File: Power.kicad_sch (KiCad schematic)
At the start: 50 parts, among them Q1 FDN86246, Q2 VOS617A-7T, T1 POE70P-50L, U1 TPS23753APW, U3 TLV431ACDBZR

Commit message: all parts geo-renamed
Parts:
- renumbered C18 to 1C1, C6 to 1C2, C5 to 1C4, C2 to 1C6, C10 to 1C7, C1 to 1C8, D4 to 1D1, D8 to 1D2, L1 to 1L1, R7 to 1R1, T1 to 1T1, C15 to 2C1, C17 to 2C11, C8 to 2C17, C14 to 2C2, C4 to 2C3, C3 to 2C4, C11 to 2C5, C13 to 2C6, C7 to 2C7, C12 to 2C8, C9 to 2C9, D3 to 2D1, D5 to 2D2, D9 to 2D3, D10 to 2D4, D6 to 2D5, D2 to 2D6, Q2 to 2Q1, Q1 to 2Q2, R18 to 2R1, R15 to 2R10, R17 to 2R11, R11 to 2R12, R8 to 2R14, R12 to 2R2, R3 to 2R21, R5 to 2R22, R1 to 2R23, R6 to 2R24, R2 to 2R25, R44 to 2R3, R9 to 2R4, R13 to 2R5, R10 to 2R6, R4 to 2R7, R16 to 2R8, R21 to 2R9, U3 to 2U1, U1 to 2U2

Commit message: properties cleanup added unique parts ID
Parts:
- 1C1, 1C2: IDAnything (none) -> 8vn418a9pwjm9b23z3yyc8b216
- 1C4: IDAnything (none) -> bccken80nrg3qa7p21h7mkcjhb
- 1C6: IDAnything (none) -> 7bve16b3npknhberdk72je696f
- 1C7: IDAnything (none) -> 3z34bstg58g3zbj6bm49cfkw50
- 1C8: IDAnything (none) -> cjbd17kqpcg079c1ae8a37wt8d
- 1D1, 1D2: IDAnything (none) -> 0r5rb2gfdykaebc85bfax6x5f2
- 1L1: IDAnything (none) -> dbn5brktrjgv9av8fstr2zcje2
- 1R1: IDAnything (none) -> f6xf1ty46ajjx8stx2pw0mweha
- 1T1: IDAnything (none) -> e7yraqef2wh4eb3jmdjy5syben; IDAnything.Var (none) -> 3.3V(erq4zdb9s4hn19b3b16cprkhzt) 5V(e7yraqef2wh4eb3jmdjy5sy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
- 2C1: IDAnything (none) -> 72ex9h1b3mkkna04sc27d3hgfj
- 2C11, 2C4: IDAnything (none) -> 812ahgx2bmk3ebs6aawcaegb7n
- 2C17: IDAnything (none) -> 59pk20syfekmjadzqyyhdbv6d4
- 2C2: IDAnything (none) -> e5kfcvbxymkwra6w8qtzj3bv2h
- 2C3: IDAnything (none) -> 3mjnpw664cjjwa4yweaynntky6
- 2C5: IDAnything (none) -> f5rakc2bw6gvc87xd8jq7r93dj
- 2C6: IDAnything (none) -> 8sc04c0ze2kfx9x5k0dj01hj4j; IDAnything.Var (none) -> 3.3V(dj5t5bmsfrgfk9cbrcgdwvhyzh) 5V(8sc04c0ze2kfx9x5k0dj01h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
- 2C7: IDAnything (none) -> 5cec8xb21wkrn9jazn0tx4yt0k
- 2C8: IDAnything (none) -> cp71jb8htmjycabjvbztj9p7aw; IDAnything.Var (none) -> 3.3V(eycg0pb0zeg5q8gbfaje4hcqkk) 5V(cp71jb8htmjycabjvbztj9p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
- 2C9: IDAnything (none) -> aqwrz00jgagpg96skhayteyvza
- 2D1: IDAnything (none) -> 3evttnjk9mjpxbyr5j5d5v7g5p
- 2D2, 2D6: IDAnything (none) -> a0668b16k0g1k959tcdyk7ydbv
- 2D3: IDAnything (none) -> 82n9ztys7pjjma8ncwczfamr62
- 2D4: IDAnything (none) -> 6yy5yjp69ph2mbefj7c13n8ymr
- 2D5: IDAnything (none) -> arf6h94jkrjsd8gf0mkfyad9b2
- 2Q1: IDAnything (none) -> ck5h9cq90mkv8ar3c2x7c5qz0c
- 2Q2: IDAnything (none) -> evtxn9kt5gk1y9gmvvka18a8hf
- 2R1: IDAnything (none) -> ftsp2a555thn6bt15g7x2jan0j
- 2R10: IDAnything (none) -> 4g20wes274jns9jencm9th8va1
- 2R11: IDAnything (none) -> 9wnk69v9dyh8a9739d0j8yezqn; IDAnything.Var (none) -> 3.3V(1yn3h33r3mkcaag9zy18qnt9dx) 5V(9wnk69v9dyh8a9739d0j8ye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
- 2R12: IDAnything (none) -> 26egdzngepjd69cx08s4ysz9m1
- 2R14, 2R4: IDAnything (none) -> 51rzmzs5b4j9y8fva05p13xw6s
- 2R2: IDAnything (none) -> 0ytke1xmp8j7w8gr20m1x2j7jv; IDAnything.Var (none) -> 3.3V(19kmsbbs8jjt68bjd3tyb4xmac) 5V(0ytke1xmp8j7w8gr20m1x2j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
- 2R21: IDAnything (none) -> 6gdsv03sw0gm694qqm04v6grhn
- 2R22: IDAnything (none) -> 52g08xz0vyhy08q0wme80j1vq0
- 2R23, 2R24: IDAnything (none) -> dyjzv1pb1rkbh96xb831vxg5z5
- 2R25: IDAnything (none) -> 7qxded0vrjg52ba46ry138eh06
- 2R3: IDAnything (none) -> 1wmdmcdgcmj9c8938zdzzabcvk
- 2R5: IDAnything (none) -> c1vc3q1ecwg38aepd291cy2avj
- 2R6: IDAnything (none) -> 3g0t5qb6k0gw2bj7sxecxs6d79
- 2R7: IDAnything (none) -> 27n3c98cw6kjv9d2ecsc87yqk3
- 2R8: IDAnything (none) -> 8katcbe2c2g6v9h87qywc7zr1y; IDAnything.Var (none) -> 3.3V(bpwqf11a58g6vacwyq9nfpvkjf) 5V(8katcbe2c2g6v9h87qywc7z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
- 2R9: IDAnything (none) -> 9p42scdygwgwrb2y4eq9ka8qyv; IDAnything.Var (none) -> 3.3V(19kmsbbs8jjt68bjd3tyb4xmac) 5V(9p42scdygwgwrb2y4eq9ka8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
- 2U1: IDAnything (none) -> 8fydhve1t4g9rbpgbwj8xzad8w
- 2U2: Availability In Stock -> (none); Check_prices https://www.snapeda.com/parts/TPS23753APW/Texas+Instruments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 -> (none); Description_1 IEEE 802.3-2005 PoE interface and Isolated Converter contro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 -> (none); IDAnything (none) -> 5jk78tnpyggbgbqs9p2kxsxakc; MF Texas Instruments -> (none); MP TPS23753APW -> (none); Package TSSOP-14 Texas Instruments -> (none); Price None -> (none); SnapEDA_Link https://www.snapeda.com/parts/TPS23753APW/Texas+Instruments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 -> (none)

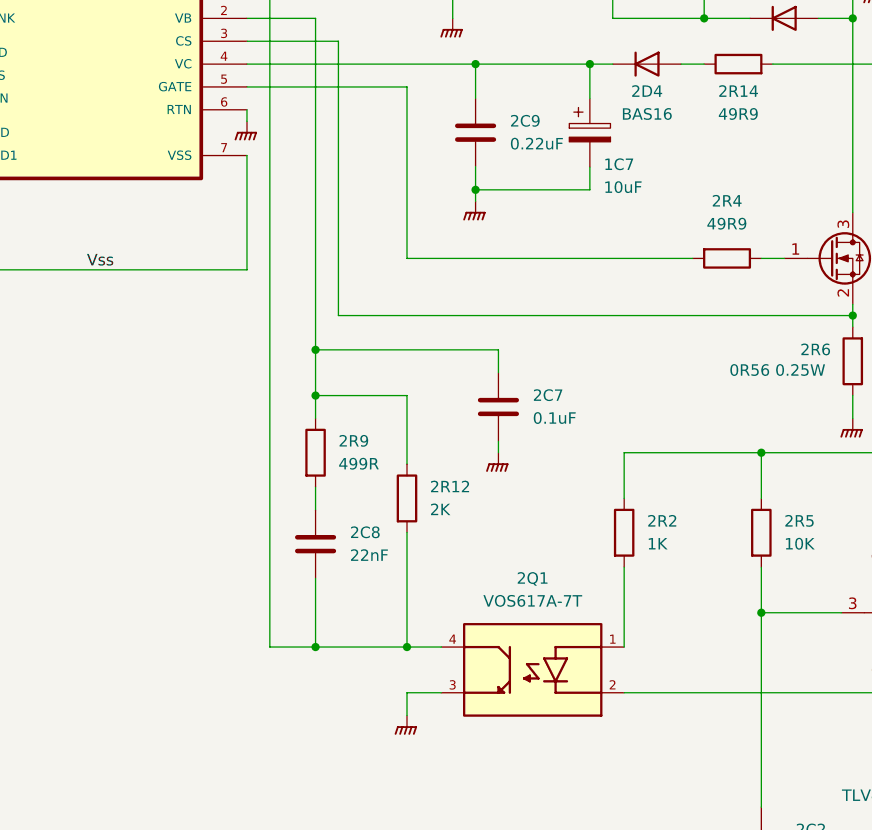
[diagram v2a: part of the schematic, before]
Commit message: added test points for PoE stage
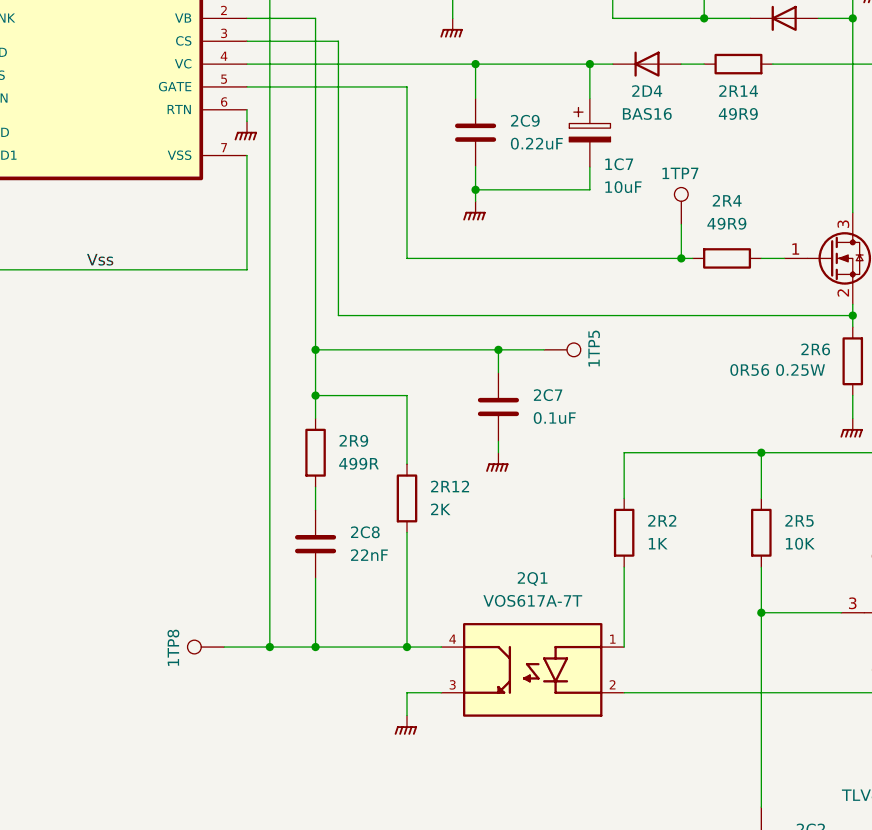
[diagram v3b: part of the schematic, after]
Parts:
- added 1TP5, 1TP7, 1TP8: TestPoint, TestPoint:TestPoint_Pad_D1.0mm, symbol Connector:TestPoint
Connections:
- net at 2C7.1, 2R12.1, 2R9.1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: now also 1TP5.1
- net at 2R4.2, 2U2.5 (GATE): now also 1TP7.1
- net at 2C8.2, 2Q1.4, 2R12.2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: now also 1TP8.1

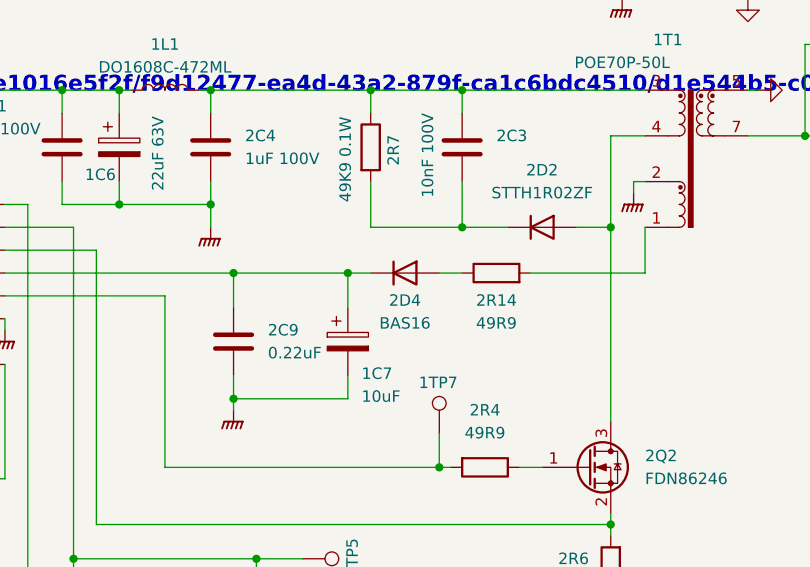
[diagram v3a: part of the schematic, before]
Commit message: fixed 2D4 polarity orientation and footprint
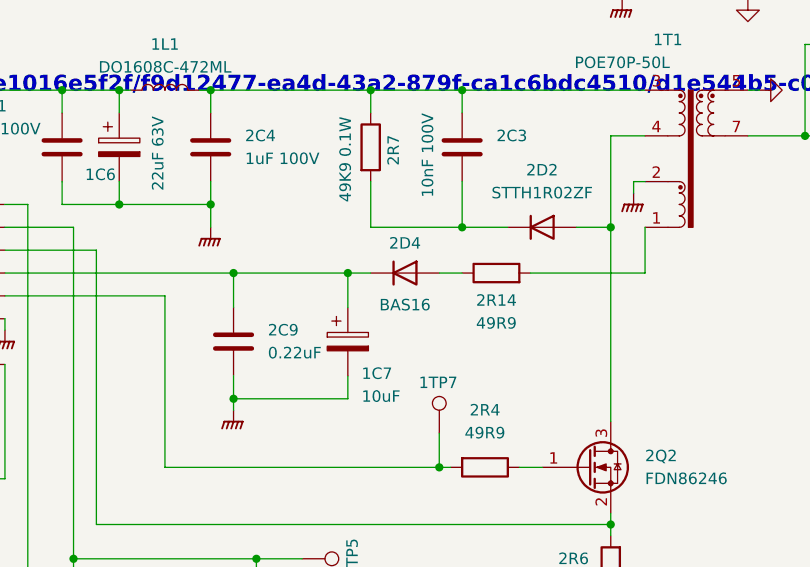
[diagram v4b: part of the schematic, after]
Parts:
- removed 2D4: BAS16, Project:SOT-23-BAS16, symbol Device:D
- added 2D4: BAS16, Package_TO_SOT_SMD:SOT-23, symbol Diode:BAS16W
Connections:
- net at 1C7.1, 2C9.1, 2U2.4 (VC): now also 2D4.3 (K)
- net at 2R14.1: now also 2D4.1 (A)
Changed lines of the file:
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@@
 	)
 	(symbol
+		(lib_id "Diode:BAS16W")
+		(at 186.69 57.15 0)
+		(unit 1)
+		(exclude_from_sim no)
+		(in_bom yes)
+		(on_board yes)
+		(dnp no)
+		(property "Reference" "2D4"
+			(at 186.69 53.848 0)
+			(effects
+				(font
+					(size 1.27 1.27)
+				)
+			)
+		)
+		(property "Value" "BAS16"
+			(at 186.69 60.706 0)
+			(effects
+				(font
+					(size 1.27 1.27)
+				)
+			)
+		)
+		(property "Footprint" "Package_TO_SOT_SMD:SOT-23"
+			(at 186.69 61.595 0)
+			(effects
+				(font
+					(size 1.27 1.27)
+				)
+				(hide yes)
+			)
+		)
+		(property "Datasheet" "Data Sheets\\BAS16_SOT_23_-3326904.pdf"
+			(at 186.69 57.15 0)
+			(effects
+				(font
+					(size 1.27 1.27)
+				)
+				(hide yes)
+			)
+		)
+		(property "Description" "100V, 0.175A, High-speed Switching Diode, SOT-323"
+			(at 186.69 57.15 0)
+			(effects
+				(font
+					(size 1.27 1.27)
+				)
+				(hide yes)
+			)
+		)
+		(property "IDAnything" "6yy5yjp69ph2mbefj7c13n8ymr"
+			(at 186.69 57.15 0)
+			(effects
+				(font
+					(size 1.27 1.27)
+				)
+				(hide yes)
+			)
+		)
+		(property "MOUSER#" "833-BAS16-TP"
+			(at 186.69 57.15 0)
+			(effects
+				(font
+					(size 1.27 1.27)
+				)
+				(hide yes)
+			)
+		)
+		(pin "3"
+		)
+		(pin "1"
+		)
+		(pin "2"
+		)
+		(instances
+			(project ""
+				(path "/4c939de5-59ef-438d-9f29-5de1016e5f2f/f9d12477-ea4d-43a2-879f-ca1c6bdc4510"
+					(reference "2D4")
+					(unit 1)
+				)
+			)
+		)
+	)
+	(symbol
 		(lib_id "Device:C_Polarized")
 		(at 154.94 43.18 0)
@@
 			)
 		)
-		(property "Datasheet" "https://assets.nexperia.com/documents/data-sheet/BAV99_SER.pdf"
+		(property "Datasheet" "Data Sheets\\bav99.pdf"
 			(at 213.36 118.11 0)
 			(effects
@@
 					(unit 1)
 				)
-			)
-		)
-	)
-	(symbol
-		(lib_id "Device:D")
-		(at 186.69 57.15 0)
-		(unit 1)
-		(exclude_from_sim no)
-		(in_bom yes)
-		(on_board yes)
-		(dnp no)
-		(property "Reference" "2D4"
-			(at 186.69 60.198 0)
-			(effects
-				(font
-					(size 1.27 1.27)
-				)
-			)
-		)
-		(property "Value" "BAS16"
-			(at 186.69 62.738 0)
-			(effects
-				(font
-					(size 1.27 1.27)
-				)
-			)
-		)
-		(property "Footprint" "Project:SOT-23-BAS16"
-			(at 186.69 57.15 0)
-			(effects
-				(font
-					(size 1.27 1.27)
-				)
-				(hide yes)
-			)
-		)
-		(property "Datasheet" "file://Data Sheets\\BAS16_SOT_23_-3326904.pdf"
-			(at 186.69 57.15 0)
-			(effects
-				(font
-					(size 1.27 1.27)
-				)
-				(hide yes)
-			)
-		)
-		(property "Description" "Diode"
-			(at 186.69 57.15 0)
-			(effects
-				(font
-					(size 1.27 1.27)
-				)
-				(hide yes)
-			)
-		)
-		(property "MOUSER#" "833-BAS16-TP"
-			(at 186.69 57.15 0)
-			(effects
-				(font
-					(size 1.27 1.27)
-				)
-				(hide yes)
-			)
-		)
-		(property "IDAnything" "6yy5yjp69ph2mbefj7c13n8ymr"
-			(at 186.69 57.15 0)
-			(effects
-				(font
-					(size 1.27 1.27)
-				)
-				(hide yes)
-			)
-		)
-		(pin "1"
-		)
-		(pin "2"
-		)
-		(instances
-			(project "ESP32PoE"
-				(path "/4c939de5-59ef-438d-9f29-5de1016e5f2f/f9d12477-ea4d-43a2-879f-ca1c6bdc4510"
-					(reference "2D4")
-					(unit 1)
-				)

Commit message: small, cosmetic fixes added project url to front silkscreen
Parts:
- 1TP5, 1TP7, 1TP8: now left out of the parts list
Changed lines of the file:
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@@
 		(unit 1)
 		(exclude_from_sim no)
-		(in_bom yes)
+		(in_bom no)
 		(on_board yes)
 		(dnp no)
@@
 		(unit 1)
 		(exclude_from_sim no)
-		(in_bom yes)
+		(in_bom no)
 		(on_board yes)
 		(dnp no)
@@
 		(unit 1)
 		(exclude_from_sim no)
-		(in_bom yes)
-		(on_board yes)
-		(dnp no)
+		(in_bom no)
+		(on_board yes)
+		(dnp no)

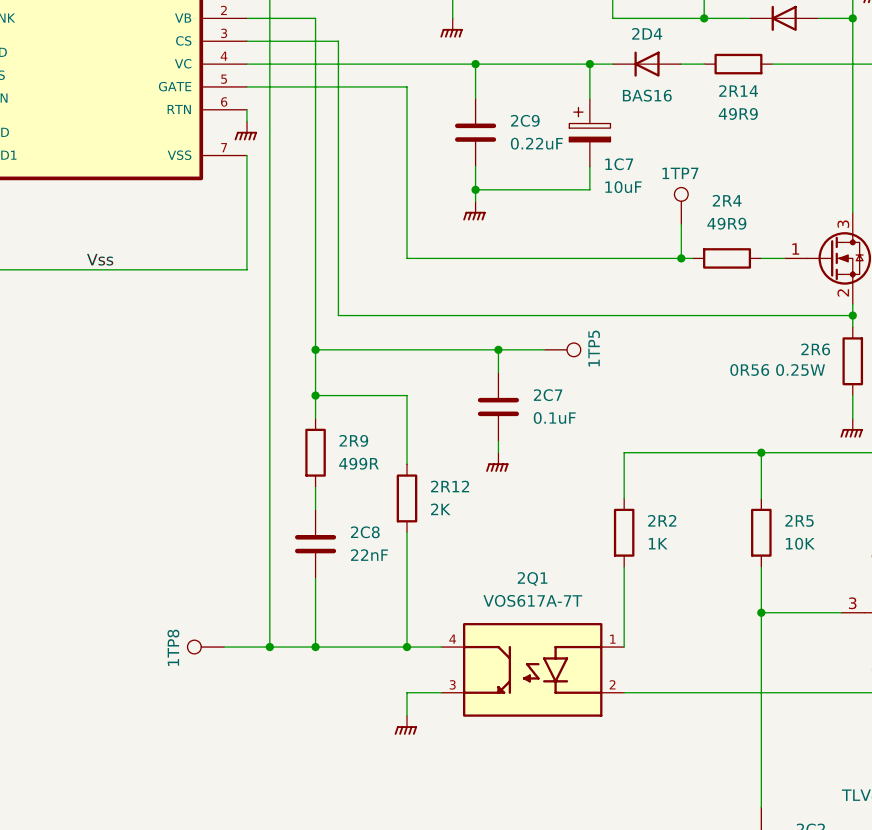
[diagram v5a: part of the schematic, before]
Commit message: ESP32 silk screen enhancement added missing part numbers finalized r0.3 work optimized Ethernet ESD diode position added second 22uF bulk updated transformer footprint courtyard enlarged supply current testpad tented bottom testpad vias for flash/ram increased bulk capacitance after efuse reverted solder paste reduction repositioning and cleanup, footprint reworks
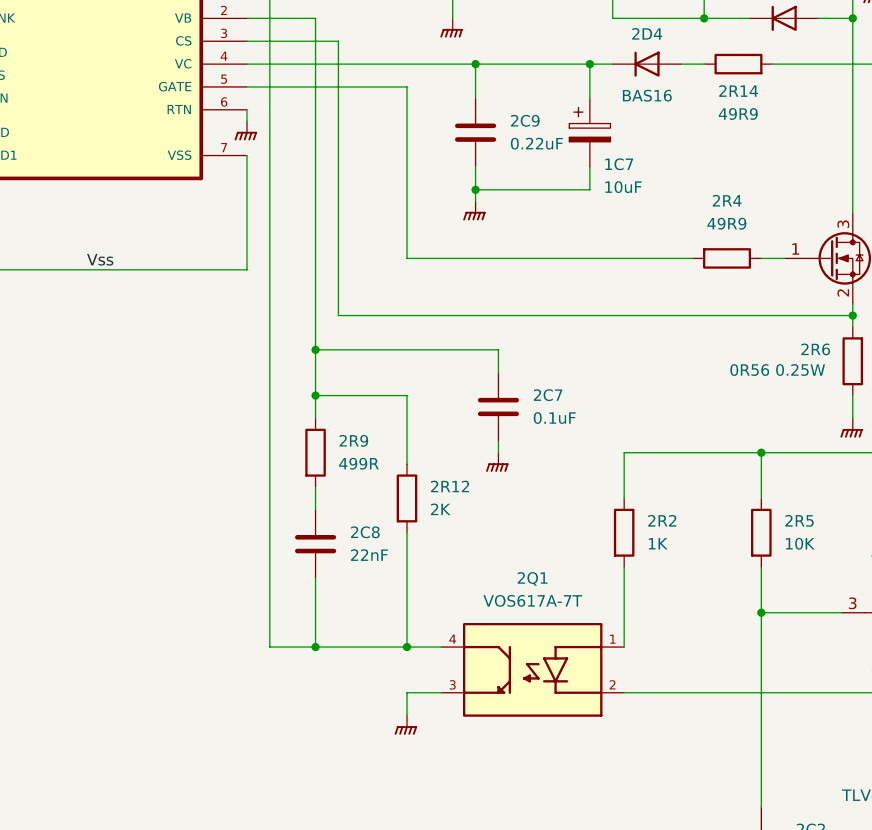
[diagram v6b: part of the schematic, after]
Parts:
- removed 1TP5, 1TP7, 1TP8: TestPoint, TestPoint:TestPoint_Pad_D1.0mm, symbol Connector:TestPoint
- 1C1, 1C2: footprint Capacitor_SMD:C_1206_3216Metric -> Capacitor_SMD:C_1210_3225Metric; IDAnything 8vn418a9pwjm9b23z3yyc8b216 -> 1c6nzaf9nyjwt94ndgc6h40zmf; MOUSER# 81-GRM31CR61A476ME5K -> 187-CL32B476MPJNNNE

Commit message: added some LCSC part numbers
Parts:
- 1D1, 1D2: LCSC# (none) -> C52151
- 1L1: LCSC# (none) -> C50326348
- 1T1: LCSC# (none) -> C20417054
- 2D1: LCSC# (none) -> C74179
- 2D2, 2D6: LCSC# (none) -> C2971384
- 2D3: LCSC# (none) -> C2500
- 2D4: LCSC# (none) -> C79997
- 2D5: LCSC# (none) -> C53278390
- 2Q1: LCSC# (none) -> C2925139
- 2Q2: LCSC# (none) -> C891118
- 2U1: LCSC# (none) -> C48586696
- 2U2: LCSC# (none) -> C92115
